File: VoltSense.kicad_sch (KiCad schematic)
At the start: 17 parts

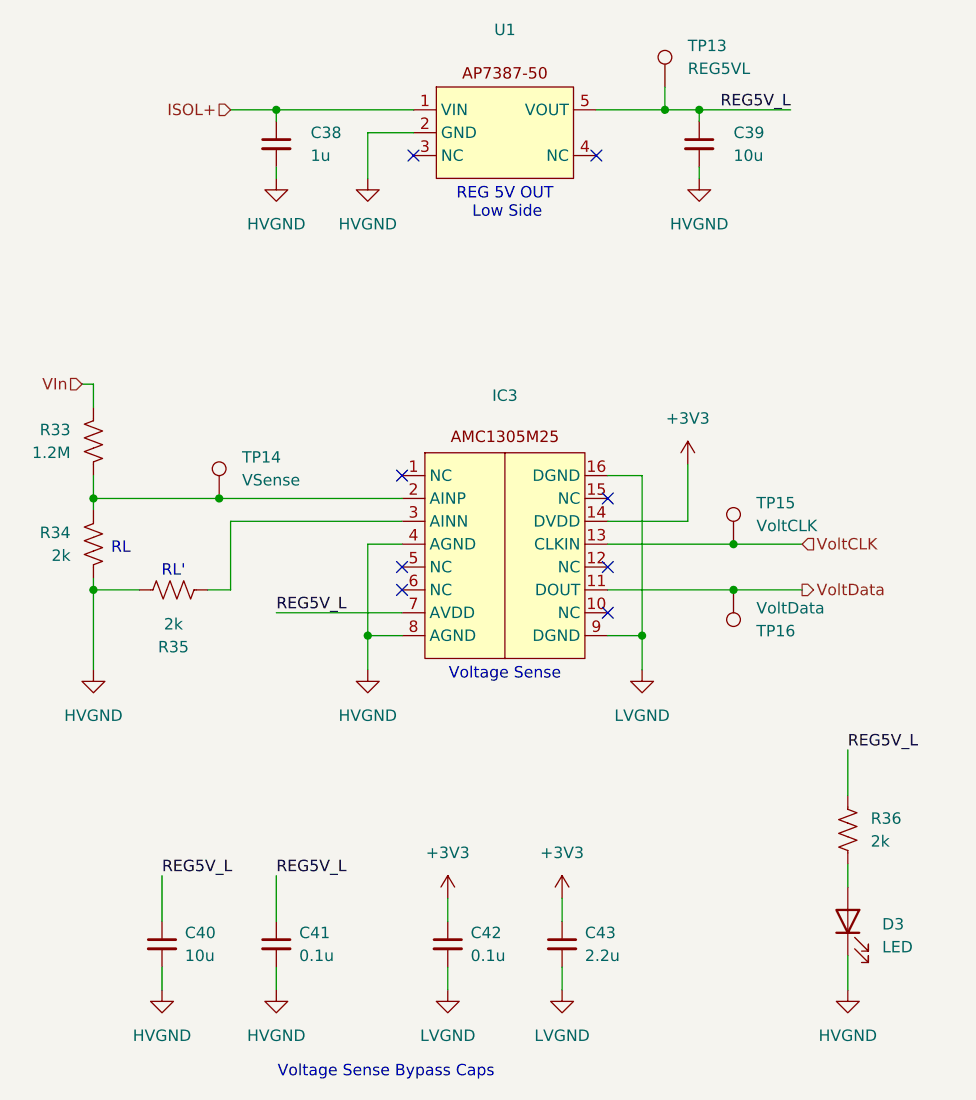
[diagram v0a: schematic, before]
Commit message: new bulk caps, new HV+,- connector placement
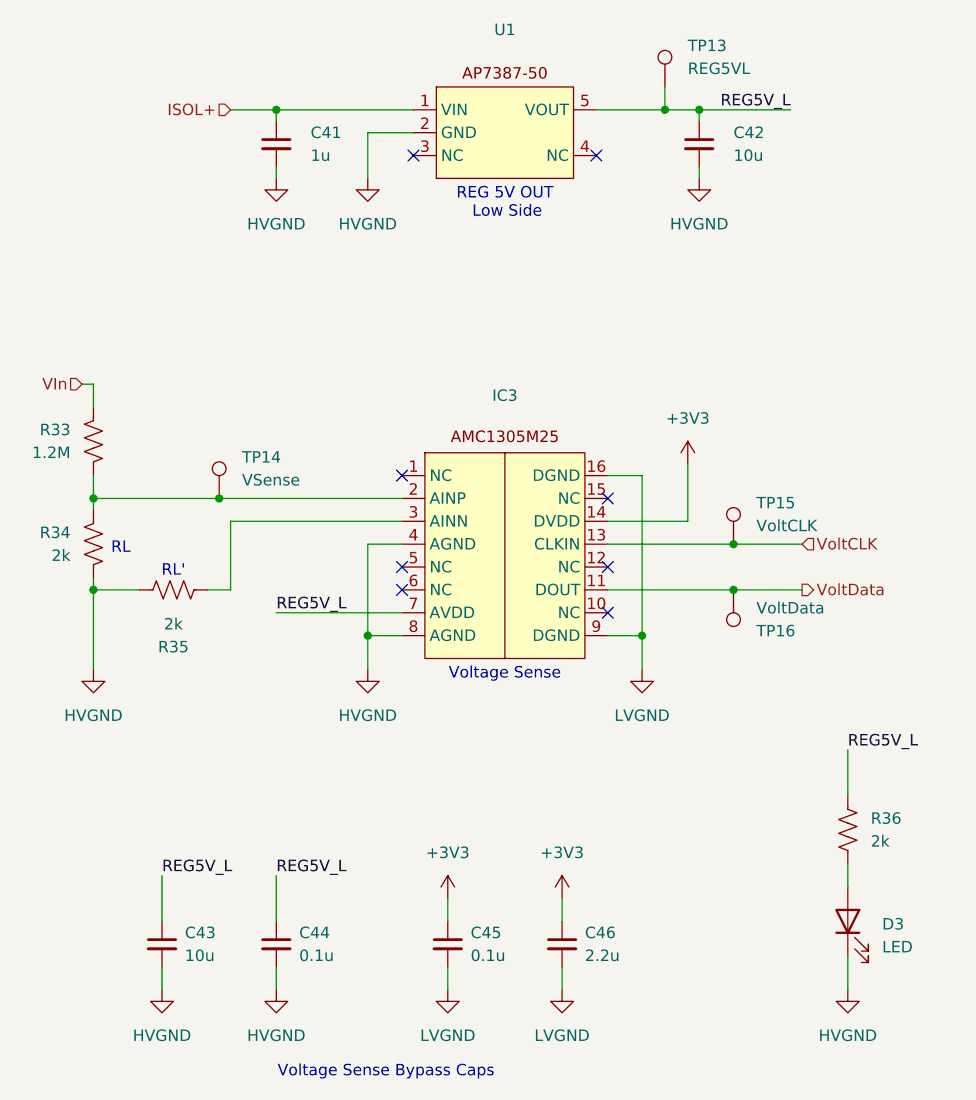
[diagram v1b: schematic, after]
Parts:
- renumbered C38 to C41, C39 to C42, C40 to C43, C41 to C44, C42 to C45, C43 to C46

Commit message: killed testpoints
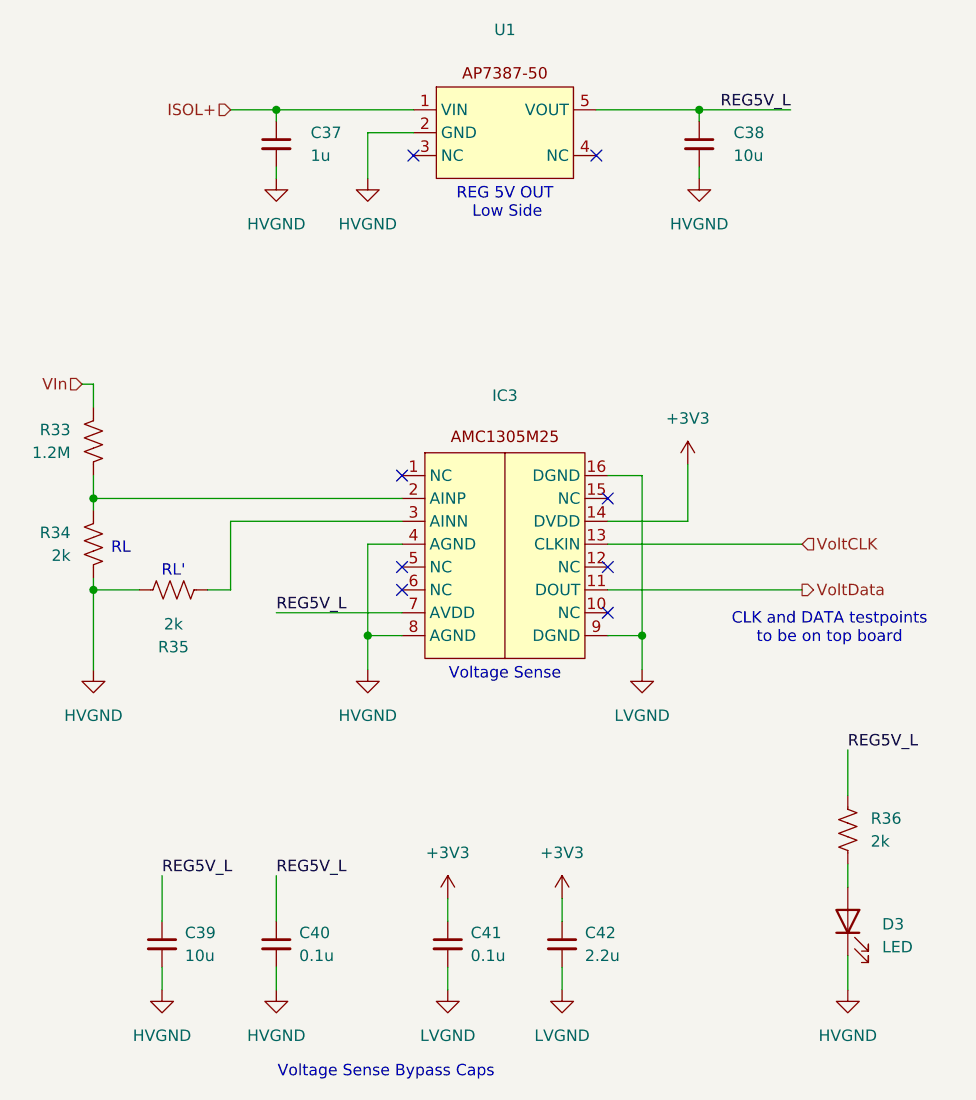
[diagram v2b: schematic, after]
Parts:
- removed TP13: REG5VL, TractionInverter:KEYSTONE_5281, symbol Connector:TestPoint
- removed TP14: VSense, TractionInverter:KEYSTONE_5281, symbol Connector:TestPoint
- removed TP15: VoltCLK, TractionInverter:KEYSTONE_5281, symbol Connector:TestPoint
- removed TP16: VoltData, TractionInverter:KEYSTONE_5281, symbol Connector:TestPoint
- renumbered C41 to C37, C42 to C38, C43 to C39, C44 to C40, C45 to C41, C46 to C42
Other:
- note added: "CLK and DATA testpoints to be on top board"
